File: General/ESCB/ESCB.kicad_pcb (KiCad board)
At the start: 2 copper layers, 3 parts, among them J1 Power_Signal, J2 Motor

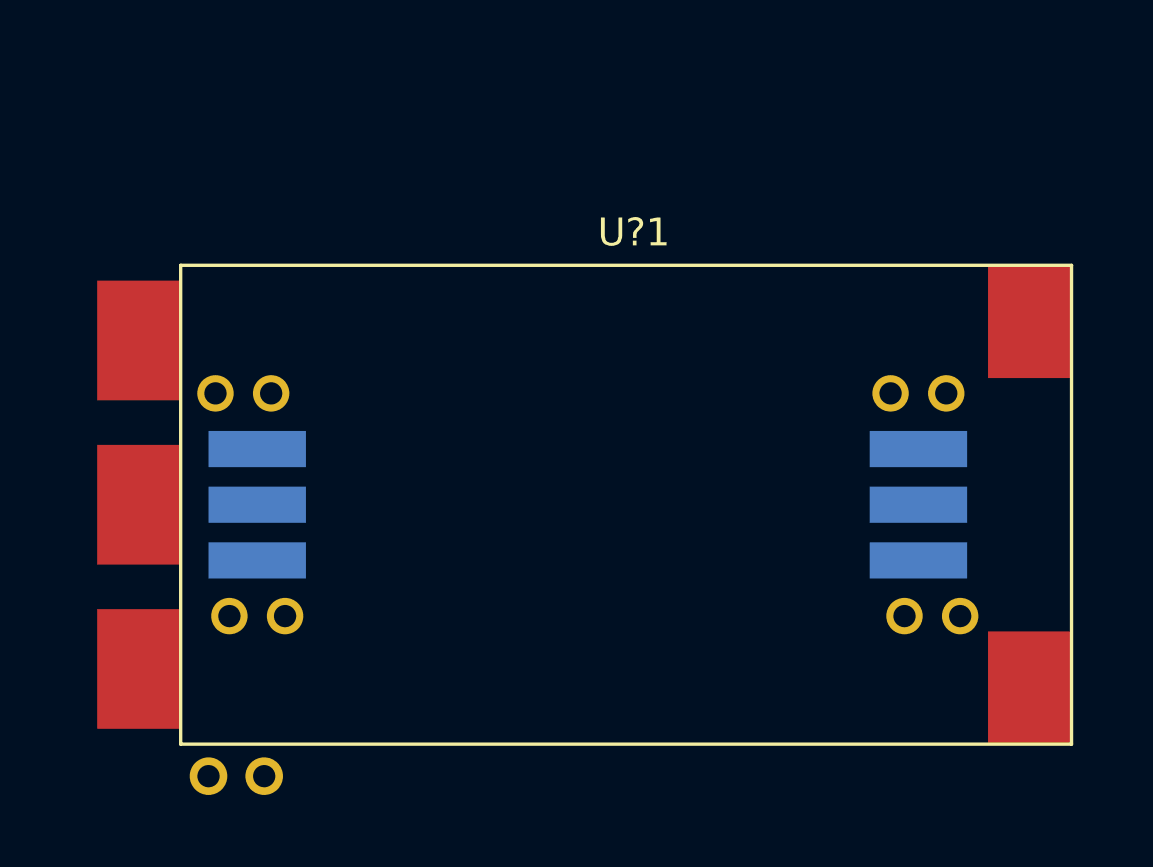
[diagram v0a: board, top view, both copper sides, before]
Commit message: ESCB Update
Added copper pores, used Saturn PCB to size vias and trace widths according to expected current draw, and routed the traces.
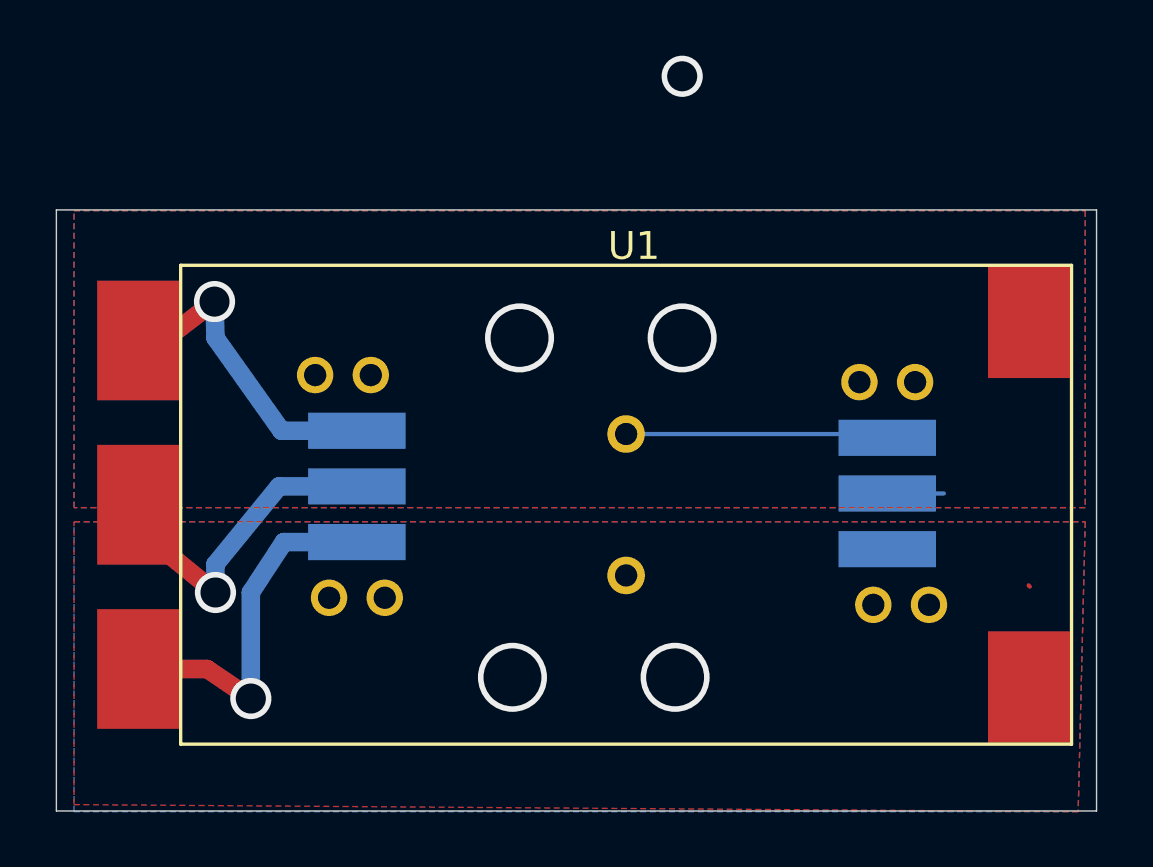
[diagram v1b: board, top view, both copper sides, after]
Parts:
- removed U?1: BESC, BESC:BESC
- added U1: BESC, BESC:BESC, F.Cu at (141.8, 101.8)
- moved J2 3.64 mm to (132.1, 101.1)
- moved J1 1.19 mm to (151.1, 101.3)
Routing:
- net Net-(J2-Pad3): track 0.00 -> 12.1 mm, vias 0 -> 1
- net Net-(J2-Pad2): track 0.00 -> 10.4 mm, vias 0 -> 1
- net Net-(J2-Pad1): track 0.00 -> 9.77 mm, vias 0 -> 1
- net Net-(J1-Pad3): track 0.00 -> 8.93 mm
- net VCC: track 0.00 -> 2.54 mm, vias 0 -> 2
- net GND: track 0.00 -> 0.06 mm, vias 0 -> 2
- net (no net): vias 0 -> 1
- added copper zone on B.Cu, net GND
- added copper zone on F.Cu, net GND
- added copper zone on B.Cu, net VCC
- added copper zone on F.Cu, net VCC
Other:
- board outline added: 37.4 x 21.6 mm
- net class Motor added: clearance 0.1524, trace_width 0.6658, via_dia 0.6096, via_drill 0.3048
- net class Power added: clearance 0.1524, trace_width 3, via_dia 0.6096, via_drill 0.3048
